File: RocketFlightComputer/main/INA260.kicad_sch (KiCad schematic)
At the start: 5 parts

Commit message: Well I added a bunch of sensors, some connectors for battery, pyro channels mosfets, etc
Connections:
- net I2CPLEX_SCL1 renamed INA260_SCL1
- net I2CPLEX_SDA1 renamed INA260_SDA1
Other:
- note added: "Max Current: 420 uA"
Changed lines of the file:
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@@
   (junction (at 140.97 78.74) (diameter 0) (color 0 0 0 0)
-  )
-  (wire (pts (xy 140.97 68.58) (xy 140.97 66.04))
-    (stroke (width 0.1524) (type solid))
   )
   (wire (pts (xy 98.425 51.435) (xy 98.425 53.975))
@@
     (effects (font (size 1.5 1.5) (thickness 0.254) bold) (justify left top))
   )
+  (text "Max Current: 420 uA" (at 90.805 102.235 0)
+    (effects (font (size 1.778 1.5113)) (justify left bottom))
+  )
   (label "BATT+" (at 80.645 43.18 0) (fields_autoplaced)
     (effects (font (size 1.2446 1.2446)) (justify left bottom))
@@
     (effects (font (size 1.2446 1.2446)) (justify left bottom))
   )
-  (hierarchical_label "I2CPLEX_SCL1" (shape input) (at 143.51 78.74 0) (fields_autoplaced)
+  (hierarchical_label "INA260_SCL1" (shape input) (at 143.51 78.74 0) (fields_autoplaced)
     (effects (font (size 1.27 1.27)) (justify left))
   )
-  (hierarchical_label "I2CPLEX_SDA1" (shape input) (at 122.555 76.2 0) (fields_autoplaced)
+  (hierarchical_label "INA260_SDA1" (shape input) (at 122.555 76.2 0) (fields_autoplaced)
     (effects (font (size 1.27 1.27)) (justify left))
   )
@@
     )
   )
-  (symbol (lib_id "power:+3.3V") (at 140.97 66.04 0) (unit 1)
+  (symbol (lib_id "power:+3.3V") (at 140.97 68.58 0) (unit 1)
     (in_bom yes) (on_board yes) (dnp no)
-    (property "Reference" "#PWR061" (at 140.97 69.85 0)
-      (effects (font (size 1.27 1.27)) hide)
-    )
-    (property "Value" "+3.3V" (at 139.065 66.675 90)
+    (property "Reference" "#PWR061" (at 140.97 72.39 0)
+      (effects (font (size 1.27 1.27)) hide)
+    )
+    (property "Value" "+3.3V" (at 139.065 69.215 90)
       (effects (font (size 1.27 1.27)) (justify left))
     )
-    (property "Footprint" "" (at 140.97 66.04 0)
-      (effects (font (size 1.27 1.27)) hide)
-    )
-    (property "Datasheet" "" (at 140.97 66.04 0)
-      (effects (font (size 1.27 1.27)) hide)
-    )
+    (property "Footprint" "" (at 140.97 68.58 0)
+      (effects (font (size 1.27 1.27)) hide)
+    )
+    (property "Datasheet" "" (at 140.97 68.58 0)
+      (effects (font (size 1.27 1.27)) hide)
+    )

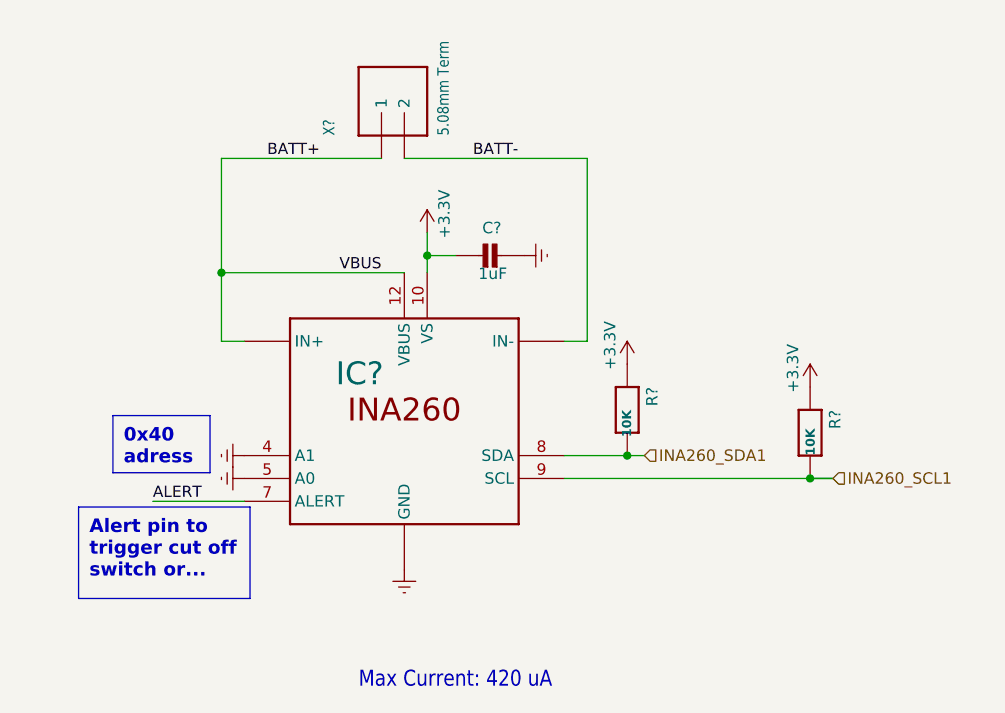
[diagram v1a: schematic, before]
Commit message: Addition of telemetry is pcb schematic
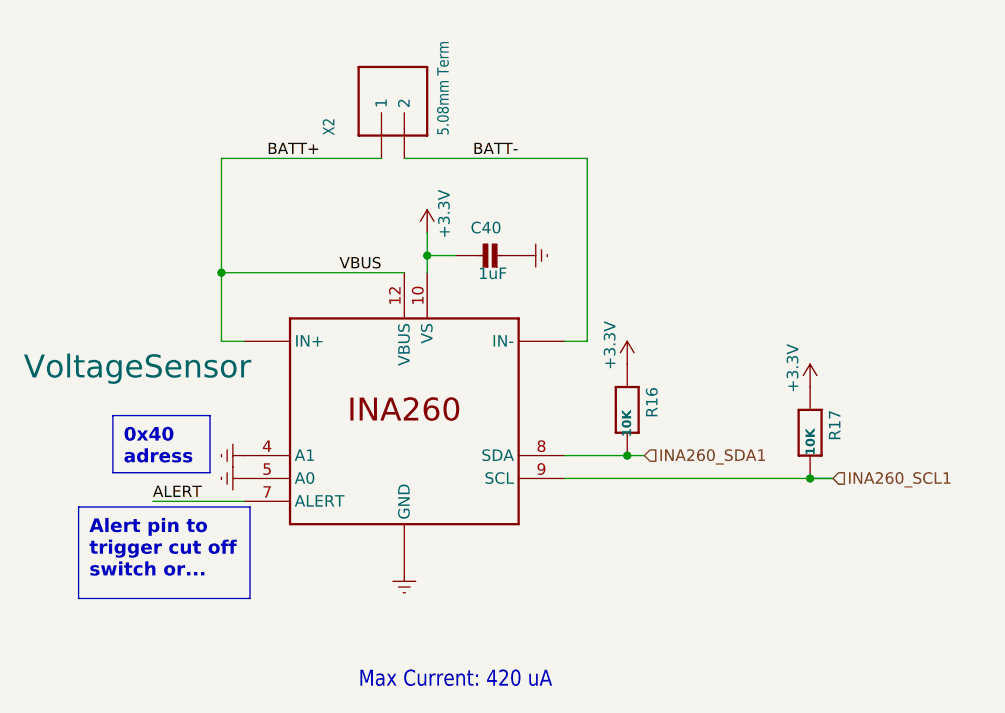
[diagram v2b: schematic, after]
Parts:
- gave numbers to parts that had none: 5

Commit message: The design is getting more mature, still did not choose if doing 4 layers or 2 layers pcb, will try to add 5v for a on board camera and trace routes for reserved pins in case of usage on another vehicle
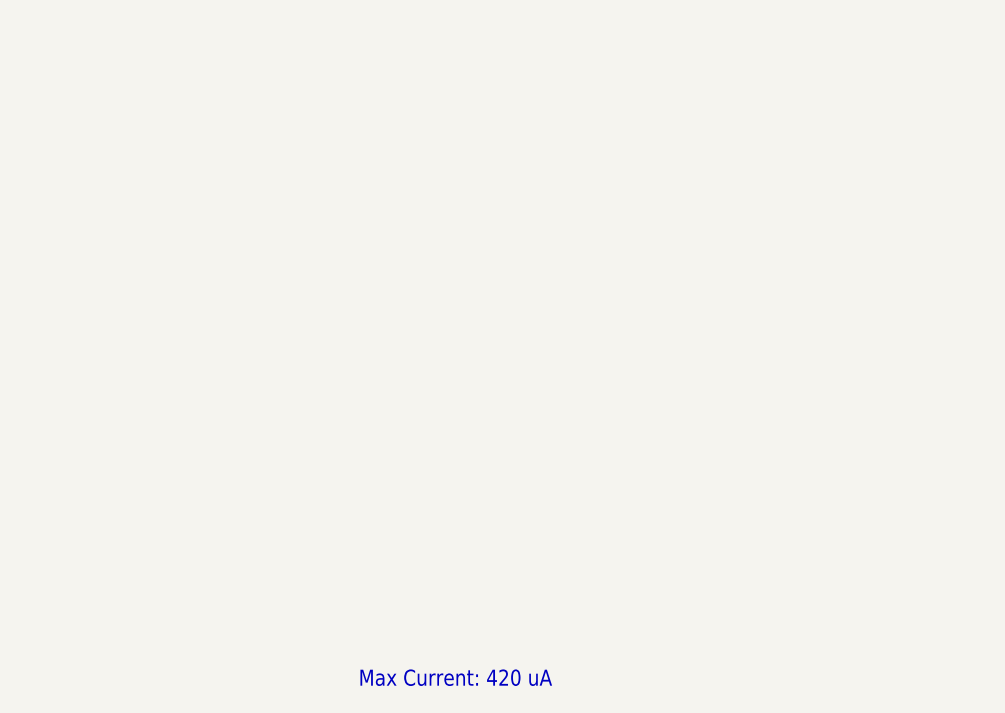
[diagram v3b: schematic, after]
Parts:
- removed C40: 1uF, Adafruit INA260:0603-NO, symbol Adafruit INA260-eagle-import:CAP_CERAMIC0603_NO
- removed R16, R17: 10K, Adafruit INA260:0603-NO, symbol Adafruit INA260-eagle-import:RESISTOR_0603_NOOUT
- removed VoltageSensor: INA260, INA260:TSSOP16, symbol Adafruit INA260-eagle-import:INA260
- removed X2: 5.08mm Term, INA260:TERMBLOCK_508_1X2, symbol Adafruit INA260-eagle-import:TERMBLOCK_1X2_5.08MM

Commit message: Camera and reserve
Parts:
- added C40: 1uF, Adafruit INA260:0603-NO, symbol Adafruit INA260-eagle-import:CAP_CERAMIC0603_NO
- added R166, R177: 10K, Adafruit INA260:0603-NO, symbol Adafruit INA260-eagle-import:RESISTOR_0603_NOOUT
- added VoltageSensor1: INA260, INA260:TSSOP16, symbol Adafruit INA260-eagle-import:INA260
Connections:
- new net +3.3V: R166.1, R177.1
- new net +5V: C40.1, VoltageSensor1.10 (VS)
- new net +7.5V: VoltageSensor1.14 (IN-), VoltageSensor1.15 (IN-), VoltageSensor1.16 (IN-)
- new net +BATT: VoltageSensor1.1 (IN+), VoltageSensor1.12 (VBUS), VoltageSensor1.2 (IN+), VoltageSensor1.3 (IN+)
- new net ALERT: VoltageSensor1.7 (ALERT)
- new net GNDREF: C40.2, VoltageSensor1.11 (GND), VoltageSensor1.13 (GND), VoltageSensor1.4 (A1), VoltageSensor1.5 (A0), VoltageSensor1.6 (GND)
- new net INA260_SCL1: R177.2, VoltageSensor1.9 (SCL)
- new net INA260_SDA1: R166.2, VoltageSensor1.8 (SDA)

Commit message: CID documentation and started the PCB editor process
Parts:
- C40, R166, R177: footprint Adafruit INA260:0603-NO -> Resistor_SMD:R_0603_1608Metric_Pad0.98x0.95mm_HandSolder
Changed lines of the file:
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@@
 			)
 		)
-		(property "Footprint" "Adafruit INA260:0603-NO"
+		(property "Footprint" "Resistor_SMD:R_0603_1608Metric_Pad0.98x0.95mm_HandSolder"
 			(at 120.65 71.12 0)
 			(effects
@@
 			)
 		)
-		(property "Footprint" "Adafruit INA260:0603-NO"
+		(property "Footprint" "Resistor_SMD:R_0603_1608Metric_Pad0.98x0.95mm_HandSolder"
 			(at 106.68 53.975 0)
 			(effects
@@
 			)
 		)
-		(property "Footprint" "Adafruit INA260:0603-NO"
+		(property "Footprint" "Resistor_SMD:R_0603_1608Metric_Pad0.98x0.95mm_HandSolder"
 			(at 140.97 73.66 0)
 			(effects

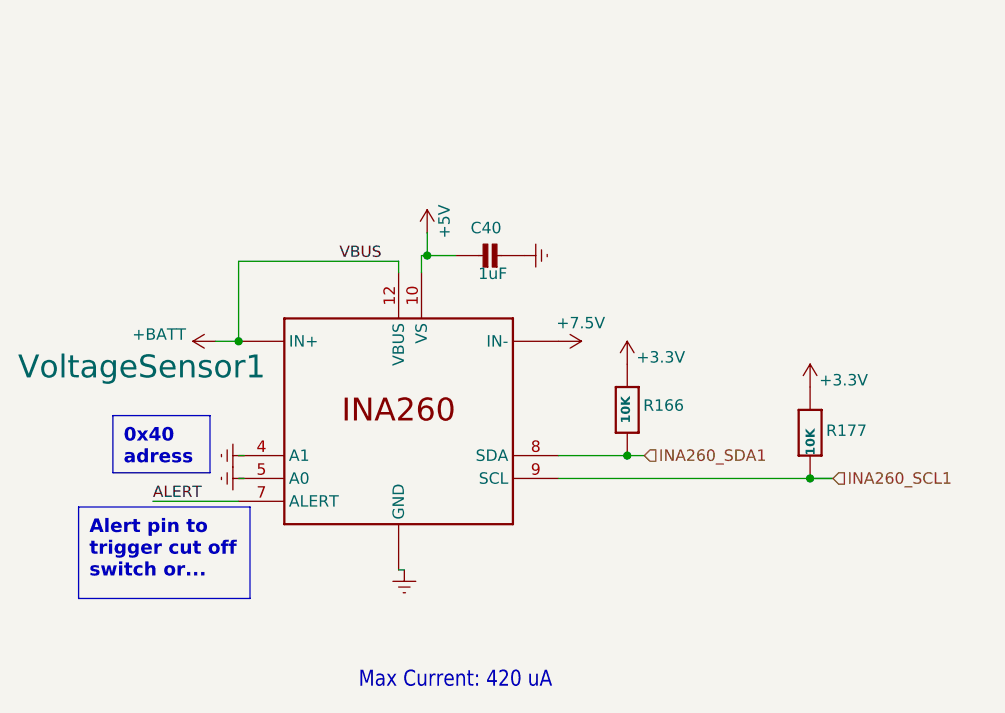
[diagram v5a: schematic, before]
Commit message: Layout of PCB mostly done
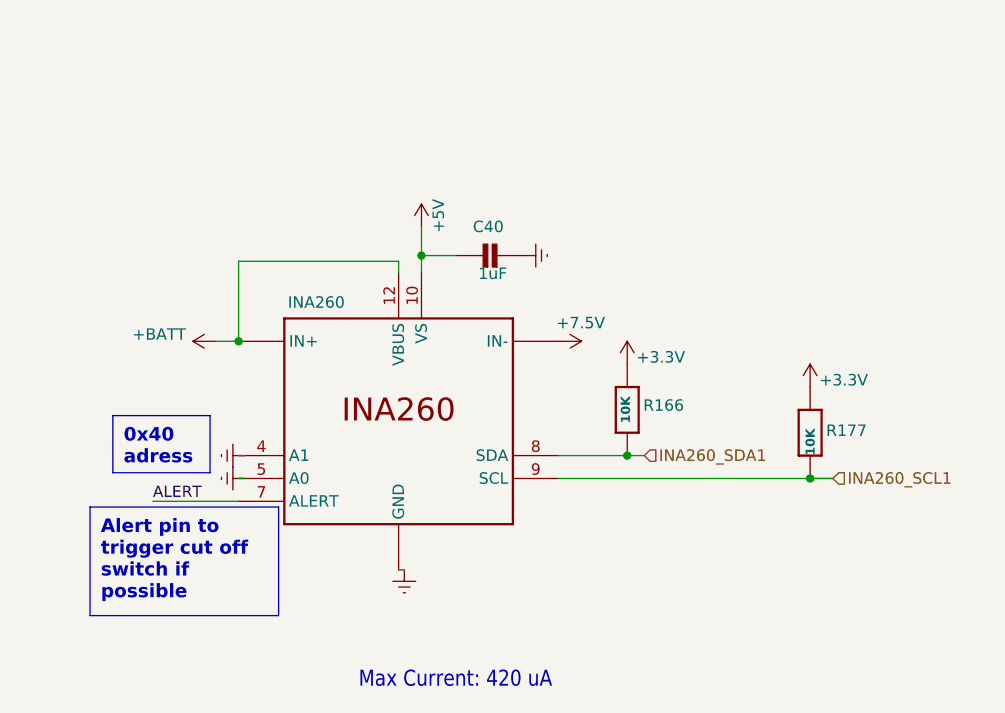
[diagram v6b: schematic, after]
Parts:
- renumbered VoltageSensor1 to INA260
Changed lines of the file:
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@@
 	(paper "A5")
+	(junction
+		(at 97.79 53.975)
+		(diameter 0)
+		(color 0 0 0 0)
+	)
 	(junction
 		(at 77.47 63.5)
@@
 	)
 	(junction
-		(at 98.425 53.975)
-		(diameter 0)
-		(color 0 0 0 0)
-	)
-	(junction
 		(at 140.97 78.74)
 		(diameter 0)
@@
 	(wire
 		(pts
-			(xy 98.425 51.435) (xy 98.425 53.975)
-		)
-		(stroke
-			(width 0)
-			(type default)
-		)
-	)
-	(wire
-		(pts
 			(xy 95.25 88.9) (xy 95.885 88.9)
 		)
@@
 	(wire
 		(pts
+			(xy 97.79 50.8) (xy 97.79 53.975)
+		)
+		(stroke
+			(width 0)
+			(type default)
+		)
+	)
+	(wire
+		(pts
 			(xy 77.47 54.61) (xy 77.47 63.5)
 		)
@@
 	(wire
 		(pts
-			(xy 97.79 53.975) (xy 98.425 53.975)
-		)
-		(stroke
-			(width 0)
-			(type default)
-		)
-	)
-	(wire
-		(pts
-			(xy 101.6 53.975) (xy 98.425 53.975)
+			(xy 97.79 53.975) (xy 101.6 53.975)
 		)
 		(stroke
@@
 		)
 	)
-	(text_box "Alert pin to trigger cut off switch or..."
-		(exclude_from_sim no)
-		(at 59.69 81.915 0)
-		(size 19.05 10.16)
+	(text_box "Alert pin to trigger cut off switch if possible"
+		(exclude_from_sim no)
+		(at 60.96 81.915 0)
+		(size 20.955 12.065)
 		(stroke
 			(width 0)
@@
 			)
 			(justify left bottom)
-		)
-	)
-	(label "VBUS"
-		(at 93.345 54.61 180)
-		(fields_autoplaced yes)
-		(effects
-			(font
-				(size 1.2446 1.2446)
-			)
-			(justify right bottom)
 		)
 	)
@@
 		(on_board yes)
 		(dnp no)
-		(property "Reference" "VoltageSensor1"
+		(property "Reference" "INA260"
 			(at 52.959 67.818 0)
 			(effects
@@
 				)
 				(justify left bottom)
+				(hide yes)
 			)
 		)
 		(property "Value" "INA260"
-			(at 95.25 71.12 0)
-			(effects
-				(font
-					(size 1.27 1.27)
-				)
-				(hide yes)
+			(at 86.106 59.182 0)
+			(effects
+				(font
+					(size 1.27 1.27)
+				)
 			)
 		)
@@
 			(project "main"
 				(path "/27195d1d-92b2-40df-ada5-3b20841577e7/125f95e9-6bcc-4b33-8d0b-519410cf48bf"
-					(reference "VoltageSensor1")
+					(reference "INA260")
 					(unit 1)
 				)
@@
 		(dnp no)
 		(property "Reference" "C40"
-			(at 106.68 50.165 90)
+			(at 106.934 50.038 90)
 			(effects
 				(font
@@
 	(symbol
 		(lib_id "power:+3.3V")
-		(at 98.425 51.435 0)
+		(at 97.79 50.8 0)
 		(unit 1)
 		(exclude_from_sim no)
@@
 		(dnp no)
 		(property "Reference" "#PWR0110"
-			(at 98.425 55.245 0)
+			(at 97.79 54.61 0)
 			(effects
 				(font
@@
 		)
 		(property "Value" "+5V"
-			(at 100.33 52.07 90)
+			(at 99.695 51.435 90)
 			(effects
 				(font
@@
 		)
 		(property "Footprint" ""
-			(at 98.425 51.435 0)
-			(effects
-				(font
-					(size 1.27 1.27)
-				)
-				(hide yes)
-			)
-		)
-		(property "Datasheet" ""
-			(at 98.425 51.435 0)
+			(at 97.79 50.8 0)
+			(effects
+				(font
+					(size 1.27 1.27)
+				)
+				(hide yes)
+			)
+		)
+		(property "Datasheet" ""
+			(at 97.79 50.8 0)
 			(effects
 				(font
@@
 		)
 		(property "Description" ""
-			(at 98.425 51.435 0)
-			(effects
-				(font
+			(at 97.79 50.8 0)
+			(effects
+				(font

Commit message: Addition of teensy example and milestone on routing completed, missing a few components to connect
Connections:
- net +5V is gone; now on net +3.3V: C40.1, INA260.10 (VS)
- net ALERT: no longer names the net of INA260.7 (ALERT)
- no-connect marks 0 -> 1
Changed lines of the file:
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@@
 		(color 0 0 0 0)
+	)
+	(no_connect
+		(at 77.47 81.28)
 	)
 	(wire
@@
 			(width 0)
 			(type default)
-		)
-	)
-	(wire
-		(pts
-			(xy 77.47 81.28) (xy 67.945 81.28)
-		)
-		(stroke
-			(width 0.1524)
-			(type solid)
 		)
 	)
@@
 			(font
 				(size 1.778 1.5113)
-			)
-			(justify left bottom)
-		)
-	)
-	(label "ALERT"
-		(at 67.945 81.28 0)
-		(fields_autoplaced yes)
-		(effects
-			(font
-				(size 1.2446 1.2446)
 			)
 			(justify left bottom)
@@
 	)
 	(symbol
+		(lib_id "power:+3.3V")
+		(at 97.79 50.8 0)
+		(unit 1)
+		(exclude_from_sim no)
+		(in_bom yes)
+		(on_board yes)
+		(dnp no)
+		(property "Reference" "#PWR0110"
+			(at 97.79 54.61 0)
+			(effects
+				(font
+					(size 1.27 1.27)
+				)
+				(hide yes)
+			)
+		)
+		(property "Value" "+3.3V"
+			(at 89.916 48.514 0)
+			(effects
+				(font
+					(size 1.27 1.27)
+				)
+				(justify left)
+			)
+		)
+		(property "Footprint" ""
+			(at 97.79 50.8 0)
+			(effects
+				(font
+					(size 1.27 1.27)
+				)
+				(hide yes)
+			)
+		)
+		(property "Datasheet" ""
+			(at 97.79 50.8 0)
+			(effects
+				(font
+					(size 1.27 1.27)
+				)
+				(hide yes)
+			)
+		)
+		(property "Description" ""
+			(at 97.79 50.8 0)
+			(effects
+				(font
+					(size 1.27 1.27)
+				)
+				(hide yes)
+			)
+		)
+		(pin "1"
+		)
+		(instances
+			(project "main"
+				(path "/27195d1d-92b2-40df-ada5-3b20841577e7/125f95e9-6bcc-4b33-8d0b-519410cf48bf"
+					(reference "#PWR0110")
+					(unit 1)
+				)
+			)
+		)
+	)
+	(symbol
 		(lib_id "Adafruit INA260-eagle-import:INA260")
 		(at 95.25 71.12 0)
@@
 					(unit 1)
 				)
-			)
-		)
-	)
-	(symbol
-		(lib_id "power:+3.3V")
-		(at 97.79 50.8 0)
-		(unit 1)
-		(exclude_from_sim no)
-		(in_bom yes)
-		(on_board yes)
-		(dnp no)
-		(property "Reference" "#PWR0110"
-			(at 97.79 54.61 0)
-			(effects
-				(font
-					(size 1.27 1.27)
-				)
-				(hide yes)
-			)
-		)
-		(property "Value" "+5V"
-			(at 99.695 51.435 90)
-			(effects
-				(font
-					(size 1.27 1.27)
-				)
-				(justify left)
-			)
-		)
-		(property "Footprint" ""
-			(at 97.79 50.8 0)
-			(effects
-				(font
-					(size 1.27 1.27)
-				)
-				(hide yes)
-			)
-		)
-		(property "Datasheet" ""
-			(at 97.79 50.8 0)
-			(effects
-				(font
-					(size 1.27 1.27)
-				)
-				(hide yes)
-			)
-		)
-		(property "Description" ""
-			(at 97.79 50.8 0)
-			(effects
-				(font
-					(size 1.27 1.27)
-				)
-				(hide yes)
-			)
-		)
-		(pin "1"
-		)
-		(instances
-			(project "main"
-				(path "/27195d1d-92b2-40df-ada5-3b20841577e7/125f95e9-6bcc-4b33-8d0b-519410cf48bf"
-					(reference "#PWR0110")
-					(unit 1)
-				)

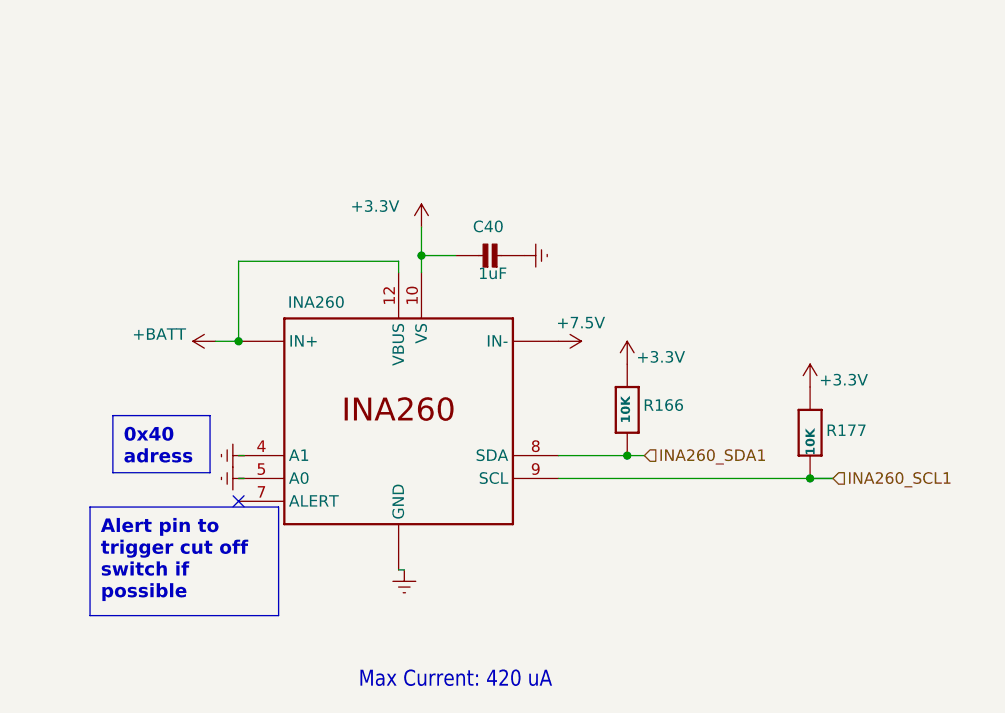
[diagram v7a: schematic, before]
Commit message: First iteration of layout finished, we could call this v0, congratulations! Need an expert to state if layer 4 and layer 3 interations are ok (pwm/ psram/i2c/uart vs power plane 7.5v and 3.3v )
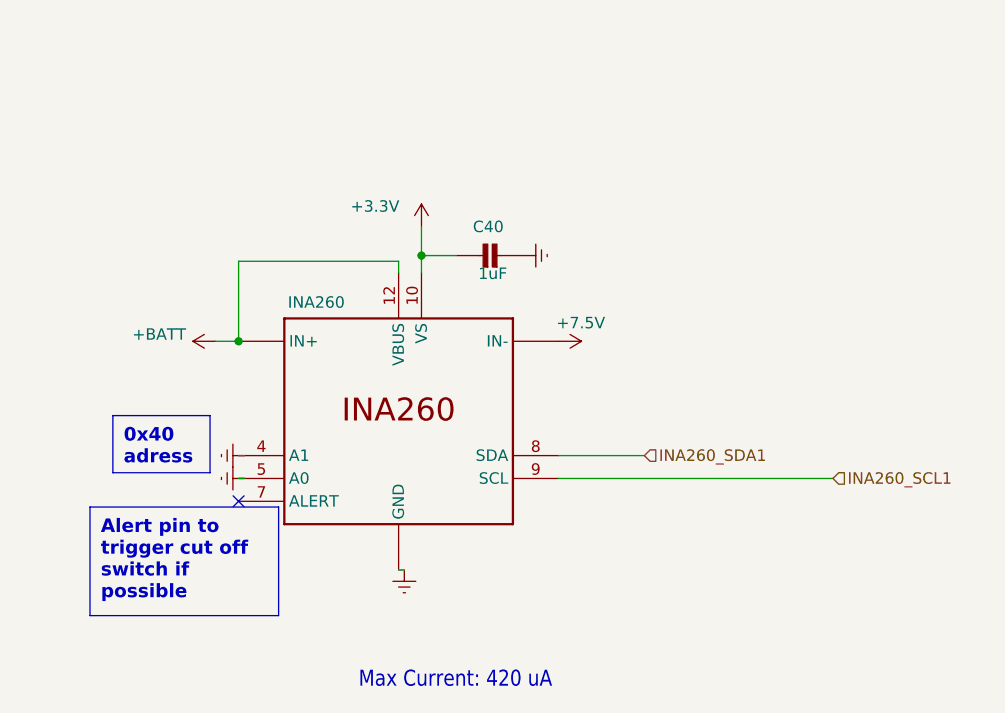
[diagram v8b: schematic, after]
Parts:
- removed R166, R177: 10K, Resistor_SMD:R_0603_1608Metric_Pad0.98x0.95mm_HandSolder, symbol Adafruit INA260-eagle-import:RESISTOR_0603_NOOUT
